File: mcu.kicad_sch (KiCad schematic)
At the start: 28 parts, among them IC1 MAX98357AETE+T, IC2 MAX98357AETE+T, SW1 SW_Push, U1 STM32WB55CGU6, Y1 32MHz, Y2 32KHz768

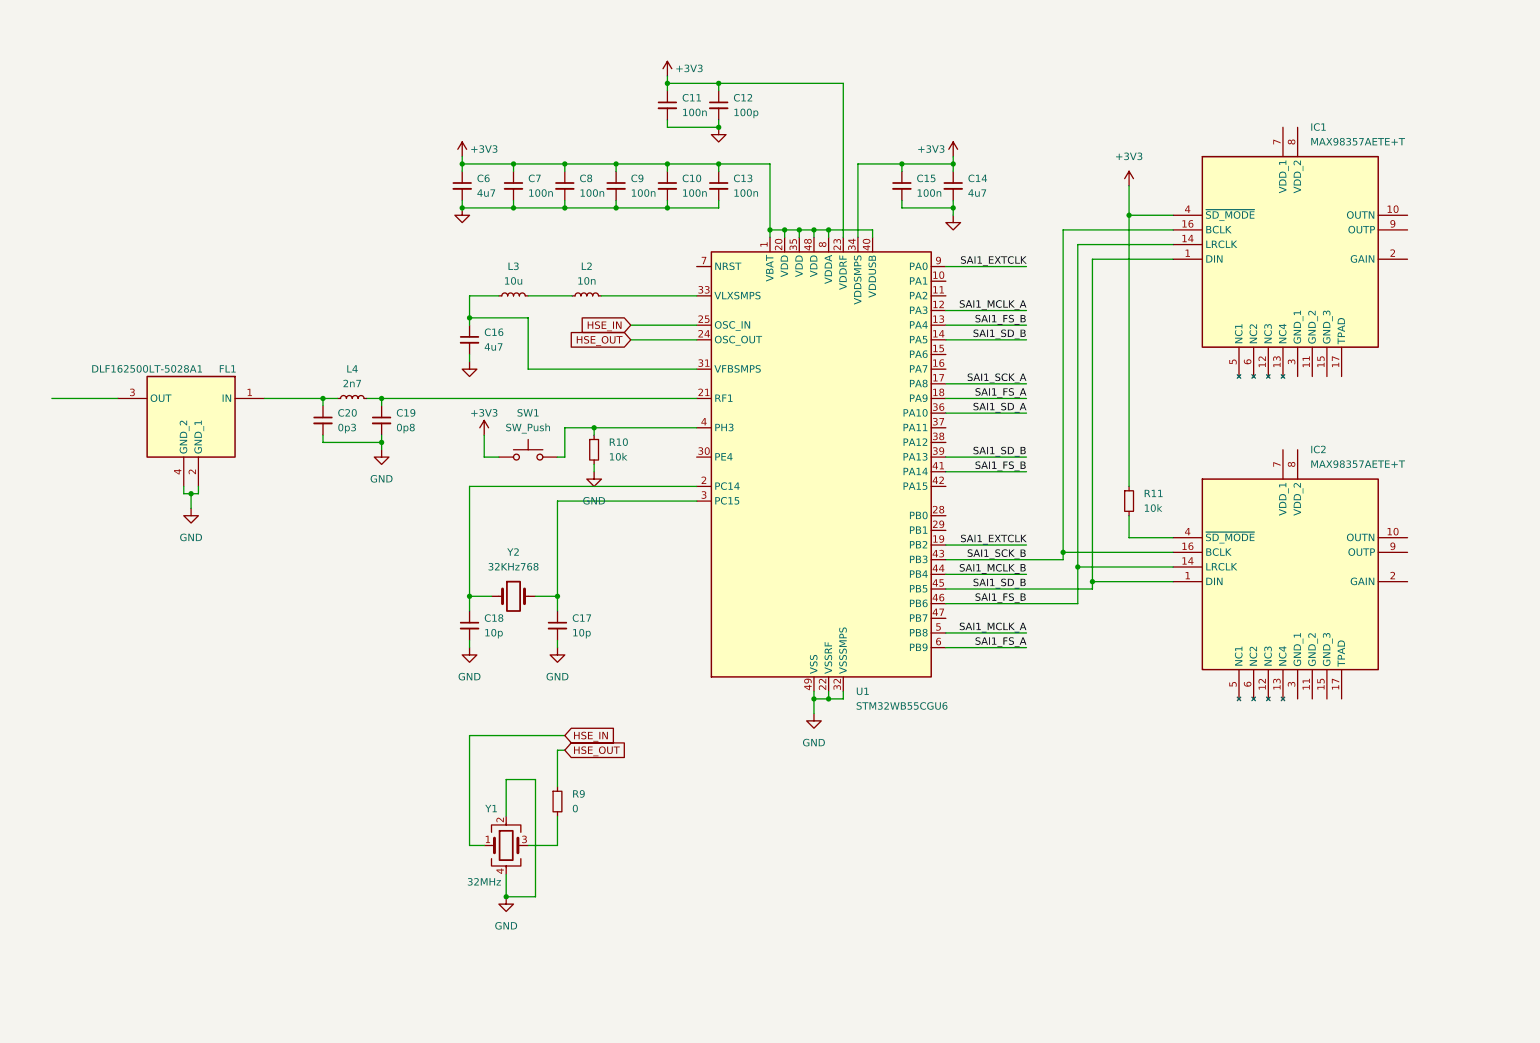
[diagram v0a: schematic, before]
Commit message: Added potentiometer and fixed amplifiers
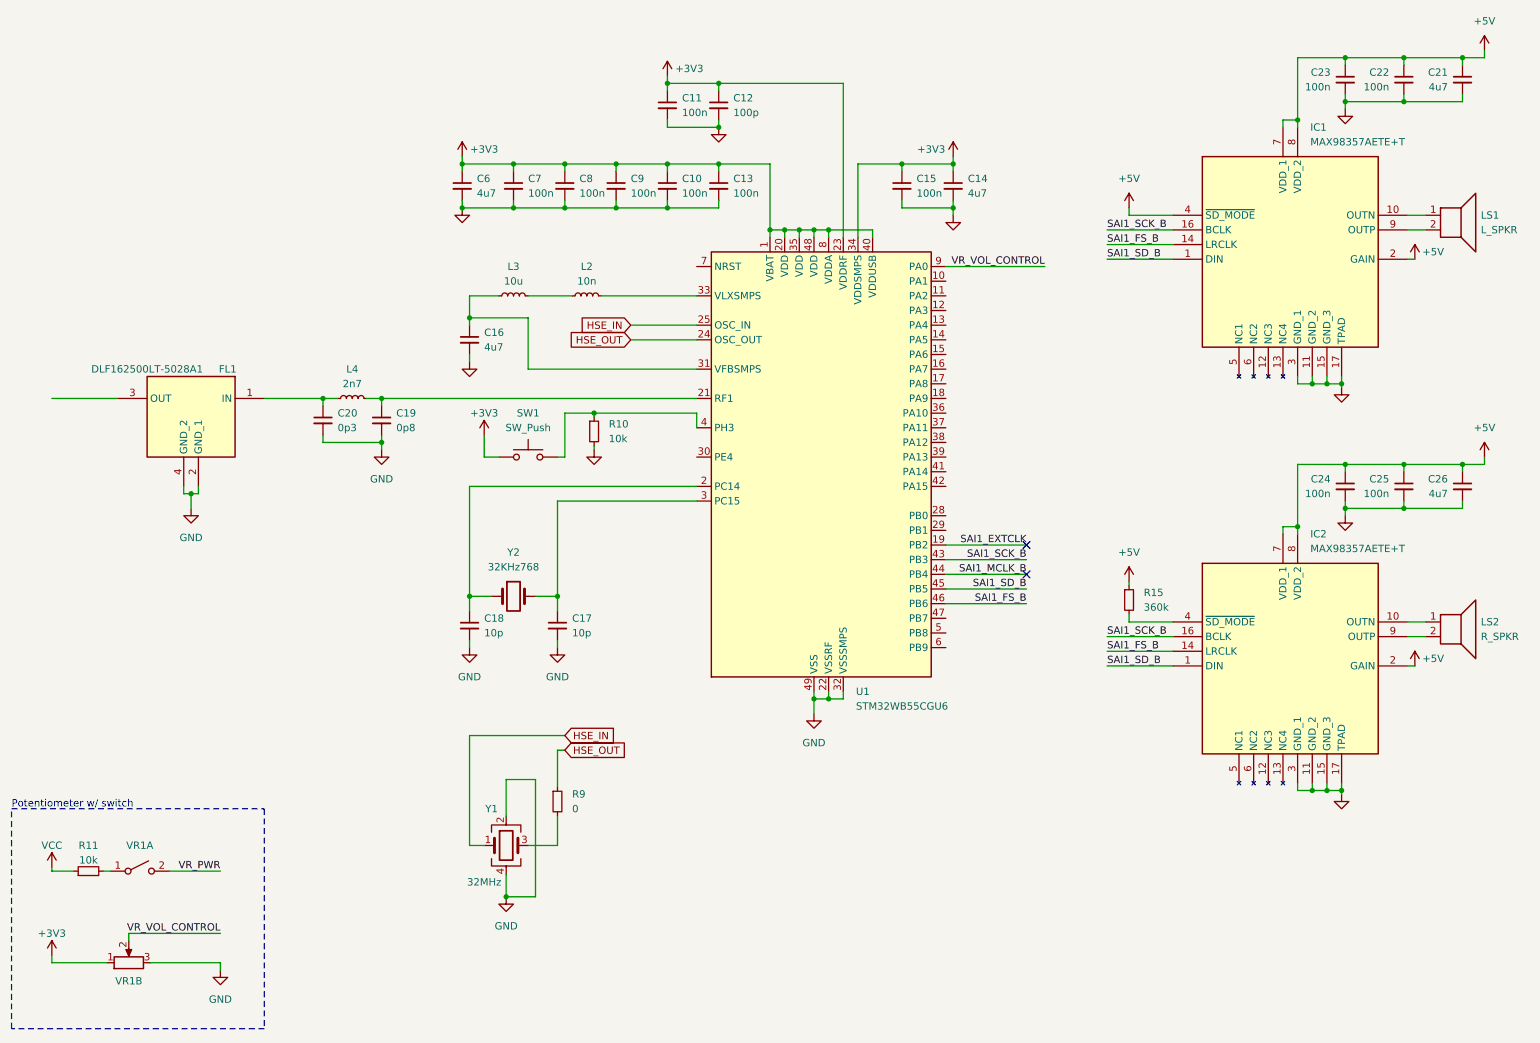
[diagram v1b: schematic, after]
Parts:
- added C21, C26: 4u7, symbol Device:C_Small
- added C22, C23, C24, C25: 100n, symbol Device:C_Small
- added LS1: L_SPKR, symbol Device:Speaker
- added LS2: R_SPKR, symbol Device:Speaker
- added R15: 360k, symbol Device:R_Small
- added VR1: ~, symbol P0915S:P0915S
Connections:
- net +3V3: now also VR1.1; no longer IC1.4 (~{SD_MODE}), R11.1
- net GND: now also IC1.11 (GND_2), IC1.15 (GND_3), IC1.17 (TPAD), IC1.3 (GND_1), IC2.11 (GND_2), IC2.15 (GND_3), IC2.17 (TPAD), IC2.3 (GND_1), C21.2, C22.2, C23.2, C24.2, C25.2, C26.2, VR1.3
- net SAI1_EXTCLK: no longer U1.9 (PA0)
- net SAI1_FS_B: no longer U1.41 (PA14)
- net SAI1_SD_B: no longer U1.14 (PA5), U1.39 (PA13)
- net at IC2.10 (OUTN): now also LS2.1
- net +5V: now reaches IC2.2 (GAIN)
- net +5V: now also IC1.2 (GAIN), IC1.4 (~{SD_MODE}), IC1.7 (VDD_1), IC1.8 (VDD_2), IC2.7 (VDD_1), IC2.8 (VDD_2), C21.1, C22.1, C23.1, C24.1, C25.1, C26.1, R15.1
- net at R11.2: now also VR1.1 (A); no longer IC2.4 (~{SD_MODE})
- net at IC2.9 (OUTP): now also LS2.2
- net at IC1.10 (OUTN): now also LS1.1
- net at IC1.9 (OUTP): now also LS1.2
- net  SAI1_FS_B: no longer names the net of U1.13 (PA4)
- net SAI1_FS_A: no longer names the net of U1.18 (PA9)
- net SAI1_FS_A: no longer U1.6 (PB9)
- net SAI1_MCLK_A: no longer names the net of U1.12 (PA3)
- net SAI1_MCLK_A: no longer U1.5 (PB8)
- net SAI1_SCK_A: no longer names the net of U1.17 (PA8)
- net SAI1_SD_A: no longer names the net of U1.36 (PA10)
- new net: IC2.4 (~{SD_MODE}), R15.2
- new net VCC: R11.1
- new net VR_PWR: VR1.2 (B)
- new net VR_VOL_CONTROL: U1.9 (PA0), VR1.2
- no-connect marks 0 -> 2
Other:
- note added: "Potentiometer w/ switch"
- moved on the sheet: IC2, R10

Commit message: Finished rev 1 of the board
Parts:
- removed C10, C11, C13, C15, C22, C23, C24, C25, C7, C8, C9: 100n, symbol Device:C_Small
- removed C12: 100p, symbol Device:C_Small
- removed C14, C16, C21, C26, C6: 4u7, symbol Device:C_Small
- removed C17, C18: 10p, symbol Device:C_Small
- removed C19: 0p8, symbol Device:C_Small
- removed C20: 0p3, symbol Device:C_Small
- removed FL1: DLF162500LT-5028A1, DLF162500LT5028A1, symbol custom_library:DLF162500LT-5028A1
- removed IC1, IC2: MAX98357AETE+T, QFN50P300X300X80-17N, symbol custom_library:MAX98357AETE+T
- removed L2: 10n, symbol Device:L_Small
- removed L3: 10u, symbol Device:L_Small
- removed L4: 2n7, symbol Device:L_Small
- removed LS1: L_SPKR, symbol Device:Speaker
- removed LS2: R_SPKR, symbol Device:Speaker
- removed R10, R11: 10k, symbol Device:R_Small
- removed R15: 360k, symbol Device:R_Small
- removed R9: 0, symbol Device:R_Small
- removed SW1: SW_Push, symbol Switch:SW_Push
- removed U1: STM32WB55CGU6, Package_DFN_QFN:QFN-48-1EP_7x7mm_P0.5mm_EP5.6x5.6mm, symbol MCU_ST_STM32WB:STM32WB55CGUx
- removed unit 1 of VR1
- removed Y1: 32MHz, symbol Device:Crystal_GND24
- removed Y2: 32KHz768, symbol Device:Crystal
- added C201, C203, C204, C205, C206, C207, C213, C214, C215: 100n, Capacitor_SMD:C_0402_1005Metric, symbol Device:C_Small
- added C202, C208: 10u, Capacitor_SMD:C_0603_1608Metric, symbol Device:C_Small
- added C209, C210: 3p3, Capacitor_SMD:C_0402_1005Metric, symbol Device:C_Small
- added C211, C212: 10p, Capacitor_SMD:C_0402_1005Metric, symbol Device:C_Small
- added D201: WIFI_LED, LED_SMD:LED_0603_1608Metric, symbol Device:LED
- added D202: PLAYING_LED, LED_SMD:LED_0603_1608Metric, symbol Device:LED
- added J201: WIFI_ANT, Connector_Coaxial:SMA_Amphenol_901-143_Horizontal, symbol Connector:Conn_Coaxial
- added L201, L202: 2n2, Inductor_SMD:L_0402_1005Metric, symbol Device:L_Small
- added R201, R204, R205: 10k, Resistor_SMD:R_0402_1005Metric, symbol Device:R_Small
- added R202: 100, Resistor_SMD:R_0402_1005Metric, symbol Device:R_Small
- added R203, R206: 5k1, Resistor_SMD:R_0402_1005Metric, symbol Device:R_Small
- added SW201: BOOT_SEL, Button_Switch_SMD:SW_SPST_SKQG_WithoutStem, symbol Switch:SW_SPST
- added U201: ESP32C3, Package_DFN_QFN:HVQFN-32-1EP_5x5mm_P0.5mm_EP3.1x3.1mm_ThermalVias, symbol ESP32C3:ESP32C3
- added U202: W25Q32JVSS, Package_SO:SOIC-8_5.23x5.23mm_P1.27mm, symbol Memory_Flash:W25Q32JVSS
- added Y201: 40MHz, Crystal:Crystal_SMD_3225-4Pin_3.2x2.5mm, symbol Device:Crystal_GND24_Small
- VR1: footprint (none) -> Internet_Radio_Speaker:Potentiometer_Alps_RK0971111Z1P; LCSC (none) -> C2687318
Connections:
- net +3V3: now also C202.1, C203.1, C205.1, C206.1, C207.1, C208.1, C215.1, L201.1, R201.1, R204.2, R205.2, U201.11 (VDD3P3_RTC), U201.17 (VDD3P3_CPU), U201.31 (VDDA), U201.32 (VDDA)
- net GND: now also C201.2, C202.2, C203.2, C204.2, C205.2, C206.2, C207.2, C208.2, C209.2, C210.2, C211.2, C212.2, C213.2, C214.2, C215.2, J201.2 (Ext), R203.1, R206.1, SW201.2 (B), U201.33 (GND), U202.4 (GND), Y201.2, Y201.4
- net VR_VOL_CONTROL: now also C214.1, U201.5 (XTAL_32K_N/IO/ANALOG)
- new net: D202.1 (K), R206.2
- new net: SW201.1 (A), U201.15 (GPIO9)
- new net AMP_SW: U201.9 (MTMS/IO/ANALOG)
- new net BAT_STAT: U201.8 (GPIO3/ANALOG)
- new net CHIP_EN: C201.1, R201.2, U201.7 (CHIP_EN)
- new net D_CAP: C204.1, L201.2, U201.2 (VDD3P3), U201.3 (VDD3P3)
- new net I2SO_BCK_OUT: U201.10 (MTDI/IO/ANALOG)
- new net I2SO_SD_OUT: U201.13 (MTDO/IO)
- new net I2SO_WS_OUT: U201.12 (MTCK/IO)
- new net LIMIT_R: R202.1, U201.30 (XTAL_P)
- new net PCB_ANTENNA: C210.1, J201.1 (In), L202.2
- new net PLAYING_LED: D202.2 (A), U201.16 (GPIO10)
- new net PU_GPIO2: R204.1, U201.6 (GPIO2/ANALOG)
- new net PU_GPIO8: R205.1, U201.14 (GPIO8)
- new net RF_ANTENNA: C209.1, L202.1, U201.1 (LNA_IN)
- new net SPICS0: U201.21 (SPICS0), U202.1 (~{CS})
- new net SPICSLK: U201.22 (SPICLK), U202.6 (CLK)
- new net SPID: U201.23 (SPID), U202.5 (DI(IO0))
- new net SPIHD: U201.19 (SPIHD), U202.7 (IO3)
- new net SPIQ: U201.24 (SPIQ), U202.2 (DO(IO1))
- new net SPIWP: U201.20 (SPIWP), U202.3 (IO2)
- new net USB_D+: U201.26 (GPIO19/USB_D+)
- new net USB_D-: U201.25 (GPIO18/USB_D-)
- new net VDD_SPI: C213.1, U201.18 (VDD_SPI), U202.8 (VCC)
- new net WIFI_CUR_R: D201.1 (K), R203.2
- new net WIFI_LED: D201.2 (A), U201.4 (XTAL_32K_P/IO/ANALOG)
- new net XTAL_N: C212.1, U201.29 (XTAL_N), Y201.3
- new net XTAL_P: C211.1, R202.2, Y201.1
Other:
- note added: "L201: 900mA"
- note added: "SPI Flash Memory"
- company: (none) -> ST
- title: (none) -> Internet Radio Speaker
- moved on the sheet: VR1B

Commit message: updated to rev 3
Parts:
- removed C202, C208: 10u, Capacitor_SMD:C_0603_1608Metric, symbol Device:C_Small
- removed C213: 100n, Capacitor_SMD:C_0402_1005Metric, symbol Device:C_Small
- removed Y201: 40MHz, Crystal:Crystal_SMD_3225-4Pin_3.2x2.5mm, symbol Device:Crystal_GND24_Small
- added C202, C208, C216: 10u, Capacitor_SMD:C_0805_2012Metric, symbol Device:C_Polarized_Small
- added J202: UART, Connector_PinSocket_2.54mm:PinSocket_1x02_P2.54mm_Vertical, symbol Connector:Conn_01x02_Pin
- added R207: 22, Resistor_SMD:R_0603_1608Metric, symbol Device:R_Small
- added SW202: RST_SW, Button_Switch_THT:SW_PUSH_6mm, symbol Switch:SW_SPST
- added Y202: 40MHz, Crystal:Crystal_SMD_HC49-SD, symbol Device:Crystal
- C201, C203, C204, C205, C206, C207, C209, C210, C211, C212, C214, C215: footprint Capacitor_SMD:C_0402_1005Metric -> Capacitor_SMD:C_0603_1608Metric
- D201, D202: footprint LED_SMD:LED_0603_1608Metric -> LED_SMD:LED_0805_2012Metric
- L201, L202: footprint Inductor_SMD:L_0402_1005Metric -> Inductor_SMD:L_0805_2012Metric
- R201, R204, R205: value 10k -> 5k1; footprint Resistor_SMD:R_0402_1005Metric -> Resistor_SMD:R_0603_1608Metric
- R202: value 100 -> 22; footprint Resistor_SMD:R_0402_1005Metric -> Resistor_SMD:R_0603_1608Metric; LCSC C25076 -> C25744
- R203, R206: footprint Resistor_SMD:R_0402_1005Metric -> Resistor_SMD:R_0603_1608Metric
- SW201: footprint Button_Switch_SMD:SW_SPST_SKQG_WithoutStem -> Button_Switch_THT:SW_PUSH_6mm
- U202: footprint Package_SO:SOIC-8_5.23x5.23mm_P1.27mm -> Package_SO:SOIC-8_3.9x4.9mm_P1.27mm
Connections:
- net +3V3: now also C202.1, C216.1
- net CHIP_EN: now also R207.1, SW202.2 (B); no longer U201.7 (CHIP_EN)
- net GND: now also C202.2, C208.2, C216.2, SW202.1 (A)
- net VDD_SPI: now also C208.1
- net XTAL_N: now also Y202.2
- net XTAL_P: now also R202.1, Y202.1; no longer R202.2
- net at U201.27 (U0RXD/IO): now also J202.1 (Pin_1)
- net at U201.28 (U0TXD/IO): now also J202.2 (Pin_2)
- net BAT_STAT: no longer names the net of U201.8 (GPIO3/ANALOG)
- net D_CAP renamed 3V3
- net I2SO_BCK_OUT renamed I2S0_BCK_OUT
- net I2SO_SD_OUT renamed I2S0_SD_OUT
- net I2SO_WS_OUT renamed I2S0_WS_OUT
- net LIMIT_R renamed XTAL_L
- net XTAL_L: now also R202.2; no longer R202.1
- new net: R207.2, U201.7 (CHIP_EN)
- no-connect marks 2 -> 1
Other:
- note removed: "L201: 900mA"

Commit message: updated to rev 4
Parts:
- removed C208: 10u, Capacitor_SMD:C_0805_2012Metric, symbol Device:C_Polarized_Small
- removed J202: UART, Connector_PinSocket_2.54mm:PinSocket_1x02_P2.54mm_Vertical, symbol Connector:Conn_01x02_Pin
- removed L201: 2n2, Inductor_SMD:L_0805_2012Metric, symbol Device:L_Small
- removed Y202: 40MHz, Crystal:Crystal_SMD_HC49-SD, symbol Device:Crystal
- added C208: 100n, Capacitor_SMD:C_0402_1005Metric, symbol Device:C_Small
- added J202: Conn_01x04, Connector_PinSocket_2.54mm:PinSocket_1x04_P2.54mm_Vertical, symbol Connector_Generic:Conn_01x04
- added JP201: EXT_3V3, Jumper:SolderJumper-2_P1.3mm_Open_RoundedPad1.0x1.5mm, symbol Jumper:SolderJumper_2_Open
- added TP201: VDD_SPI_TP, TestPoint:TestPoint_Pad_D1.5mm, symbol Connector:TestPoint_Small
- added Y201: 40MHz 10p5, Crystal:Crystal_SMD_3225-4Pin_3.2x2.5mm, symbol Device:Crystal_GND24
- C201, C203, C204, C205, C206, C207, C214, C215: footprint Capacitor_SMD:C_0603_1608Metric -> Capacitor_SMD:C_0402_1005Metric; JLCPCB Part # (none) -> C1525; LCSC C1525 -> (none)
- C202, C216: footprint Capacitor_SMD:C_0805_2012Metric -> Capacitor_SMD:C_0603_1608Metric; JLCPCB Part # (none) -> C96446
- C209, C210: value 3p3 -> 1p8; footprint Capacitor_SMD:C_0603_1608Metric -> Capacitor_SMD:C_0402_1005Metric; JLCPCB Part # (none) -> C1553; LCSC C1565 -> (none)
- C211, C212: value 10p -> 12p; footprint Capacitor_SMD:C_0603_1608Metric -> Capacitor_SMD:C_0402_1005Metric; JLCPCB Part # (none) -> C1547; LCSC C32949 -> (none)
- D201: JLCPCB Part # (none) -> C2297; LCSC C72041 -> (none)
- D202: JLCPCB Part # (none) -> C2296; LCSC C72038 -> (none)
- J201: footprint Connector_Coaxial:SMA_Amphenol_901-143_Horizontal -> Internet_Radio_Speaker:Texas_SWRA117D_2.4GHz_Right
- L202: value 2n2 -> 2n7; footprint Inductor_SMD:L_0805_2012Metric -> Inductor_SMD:L_0402_1005Metric; JLCPCB Part # (none) -> C77108; LCSC C97985 -> (none)
- R201, R204, R205: footprint Resistor_SMD:R_0603_1608Metric -> Resistor_SMD:R_0402_1005Metric; JLCPCB Part # (none) -> C25905; LCSC C25744 -> (none)
- R202, R207: value 22 -> 22R; footprint Resistor_SMD:R_0603_1608Metric -> Resistor_SMD:R_0402_1005Metric; JLCPCB Part # (none) -> C25092; LCSC C25744 -> (none)
- R203, R206: value 5k1 -> 1k; footprint Resistor_SMD:R_0603_1608Metric -> Resistor_SMD:R_0402_1005Metric; JLCPCB Part # (none) -> C11702; LCSC C25905 -> (none)
- SW201, SW202: JLCPCB Part # (none) -> C2889001; LCSC C318884 -> (none)
- U202: value W25Q32JVSS -> W25Q128JVPIQ; footprint Package_SO:SOIC-8_3.9x4.9mm_P1.27mm -> Package_SON:WSON-8-1EP_6x5mm_P1.27mm_EP3.4x4.3mm; JLCPCB Part # (none) -> C190862; LCSC C179173 -> (none); now not fitted; now left out of the parts list
- VR1: JLCPCB Part # (none) -> C2687318; LCSC C2687318 -> (none)
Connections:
- net 3V3 is gone; now on net +3V3: C204.1, U201.2 (VDD3P3), U201.3 (VDD3P3)
- net +3V3: now also R201.2, J202.1 (Pin_1), JP201.2 (B); no longer R201.1
- net CHIP_EN: now also R201.1; no longer R201.2
- net GND: now also C211.1, C212.1, R206.2, SW201.1 (A), C208.2, J202.2 (Pin_2), Y201.2, Y201.4; no longer C211.2, C212.2, R206.1, SW201.2 (B)
- net VDD_SPI: now also C208.1, JP201.1 (A), TP201.1
- net WIFI_LED: now also U201.8 (GPIO3/ANALOG); no longer U201.4 (XTAL_32K_P/IO/ANALOG)
- net XTAL_N: now also C211.2, Y201.1; no longer C212.1
- net XTAL_P: now also C212.2, Y201.3; no longer C211.1
- net at D202.1 (K): now also R206.1; no longer R206.2
- net BOOT_SEL: now reaches U201.15 (GPIO9)
- net BOOT_SEL: now also SW201.2 (B); no longer SW201.1 (A)
- net UART_RX: now reaches U201.27 (U0RXD/IO)
- net UART_RX: now also J202.3 (Pin_3)
- net UART_TX: now reaches U201.28 (U0TXD/IO)
- net UART_TX: now also J202.4 (Pin_4)
- net WIFI_CUR_R: no longer names the net of D201.1 (K), R203.2
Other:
- note added: "ESP32C3 Microcontroller"
- note added: "Status LEDs"
- note added: "Switches"
- moved on the sheet: C201, C202, C203, C204, C205, C206, C207, C209, C210, C211, C212, C214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
